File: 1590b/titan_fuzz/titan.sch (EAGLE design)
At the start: 60 parts, among them J1 DC_MONO, Q1 2N5088, Q2 2N5088, Q3 2N5088, Q4 2N5088

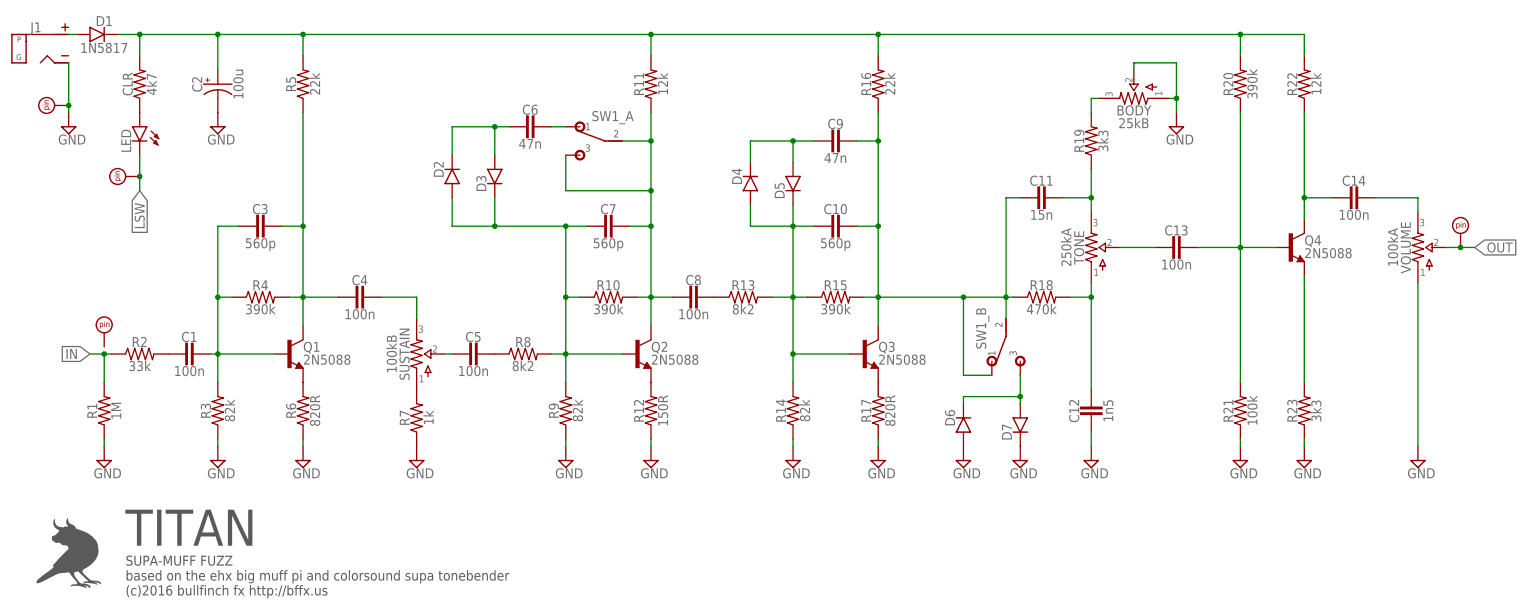
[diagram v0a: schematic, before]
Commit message: updated library + logos
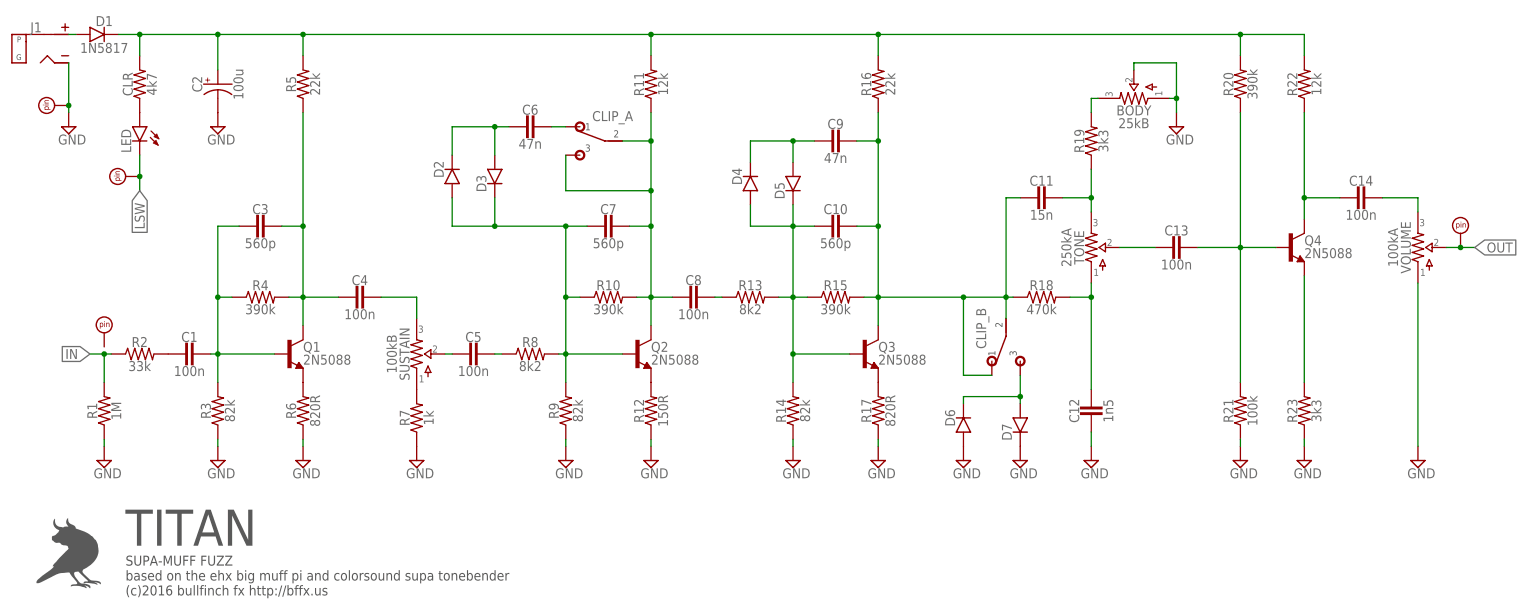
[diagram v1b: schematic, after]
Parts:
- renumbered SW1 to CLIP
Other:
- moved on the sheet: C14, R13, R8
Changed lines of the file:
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@@
 <setting verticaltext="up"/>
 </settings>
-<grid distance="0.05" unitdist="inch" unit="inch" style="lines" multiple="2" display="no" altdistance="0.01" altunitdist="inch" altunit="inch"/>
+<grid distance="0.1" unitdist="inch" unit="inch" style="lines" multiple="1" display="no" altdistance="0.01" altunitdist="inch" altunit="inch"/>
 <layers>
 <layer number="1" name="Top" color="4" fill="1" visible="no" active="no"/>
@@
 <part name="GND11" library="supply pins" deviceset="GND" device=""/>
 <part name="GND12" library="supply pins" deviceset="GND" device=""/>
-<part name="SW1" library="switches" deviceset="DPDT" device="PADS"/>
+<part name="CLIP" library="switches" deviceset="DPDT" device="PADS"/>
 <part name="BF1" library="logos" deviceset="BULLFINCH" device=""/>
 <part name="IN" library="supply pins" deviceset="PAD" device="SQR"/>
@@
 <instance part="R7" gate="G$1" x="77.47" y="34.29" rot="R90"/>
 <instance part="C5" gate="G$1" x="87.63" y="45.72"/>
-<instance part="R8" gate="G$1" x="96.52" y="45.72"/>
+<instance part="R8" gate="G$1" x="97.79" y="45.72"/>
 <instance part="R9" gate="G$1" x="104.14" y="35.56" rot="R90"/>
 <instance part="Q2" gate="G$1" x="116.84" y="45.72"/>
@@
 <instance part="R10" gate="G$1" x="111.76" y="55.88"/>
 <instance part="C8" gate="G$1" x="127" y="55.88"/>
-<instance part="R13" gate="G$1" x="135.89" y="55.88"/>
+<instance part="R13" gate="G$1" x="137.16" y="55.88"/>
 <instance part="C7" gate="G$1" x="111.76" y="68.58"/>
 <instance part="C6" gate="G$1" x="97.79" y="86.36"/>
@@
 <instance part="R22" gate="G$1" x="236.22" y="93.98" rot="R90"/>
 <instance part="R23" gate="G$1" x="236.22" y="35.56" rot="R90"/>
-<instance part="C14" gate="G$1" x="245.11" y="73.66"/>
+<instance part="C14" gate="G$1" x="246.38" y="73.66"/>
 <instance part="VOLUME" gate="G$1" x="256.54" y="64.77"/>
 <instance part="J1" gate="DC" x="10.16" y="100.33"/>
@@
 <instance part="GND11" gate="GND" x="175.26" y="26.67"/>
 <instance part="GND12" gate="GND" x="185.42" y="26.67"/>
-<instance part="SW1" gate="_A" x="109.22" y="83.82" rot="MR270"/>
-<instance part="SW1" gate="_B" x="182.88" y="46.99" rot="MR180"/>
+<instance part="CLIP" gate="_A" x="109.22" y="83.82" rot="MR270"/>
+<instance part="CLIP" gate="_B" x="182.88" y="46.99" rot="MR180"/>
 <instance part="BF1" gate="G$1" x="15.24" y="10.16"/>
 <instance part="IN" gate="G$1" x="21.59" y="46.99"/>
@@
 <pinref part="C8" gate="G$1" pin="1"/>
 <pinref part="R13" gate="G$1" pin="1"/>
+<wire x1="132.08" y1="55.88" x2="130.81" y2="55.88" width="0.1524" layer="91"/>
 </segment>
 </net>
@@
 <pinref part="C5" gate="G$1" pin="1"/>
 <pinref part="R8" gate="G$1" pin="1"/>
+<wire x1="92.71" y1="45.72" x2="91.44" y2="45.72" width="0.1524" layer="91"/>
 </segment>
 </net>
@@
 <junction x="119.38" y="55.88"/>
 <wire x1="119.38" y1="55.88" x2="123.19" y2="55.88" width="0.1524" layer="91"/>
-<pinref part="SW1" gate="_A" pin="2"/>
+<pinref part="CLIP" gate="_A" pin="2"/>
 <wire x1="114.3" y1="83.82" x2="119.38" y2="83.82" width="0.1524" layer="91"/>
 <junction x="119.38" y="83.82"/>
-<pinref part="SW1" gate="_A" pin="3"/>
+<pinref part="CLIP" gate="_A" pin="3"/>
 <wire x1="104.14" y1="81.28" x2="104.14" y2="74.93" width="0.1524" layer="91"/>
 <wire x1="104.14" y1="74.93" x2="119.38" y2="74.93" width="0.1524" layer="91"/>
@@
 <pinref part="R8" gate="G$1" pin="2"/>
 <pinref part="Q2" gate="G$1" pin="B"/>
-<wire x1="101.6" y1="45.72" x2="104.14" y2="45.72" width="0.1524" layer="91"/>
+<wire x1="102.87" y1="45.72" x2="104.14" y2="45.72" width="0.1524" layer="91"/>
 <wire x1="104.14" y1="45.72" x2="114.3" y2="45.72" width="0.1524" layer="91"/>
 <wire x1="104.14" y1="68.58" x2="104.14" y2="55.88" width="0.1524" layer="91"/>
@@
 <wire x1="182.88" y1="73.66" x2="185.42" y2="73.66" width="0.1524" layer="91"/>
 <junction x="182.88" y="55.88"/>
-<pinref part="SW1" gate="_B" pin="2"/>
+<pinref part="CLIP" gate="_B" pin="2"/>
 <wire x1="175.26" y1="55.88" x2="182.88" y2="55.88" width="0.1524" layer="91"/>
 <wire x1="182.88" y1="55.88" x2="182.88" y2="52.07" width="0.1524" layer="91"/>
-<pinref part="SW1" gate="_B" pin="1"/>
+<pinref part="CLIP" gate="_B" pin="1"/>
 <wire x1="180.34" y1="41.91" x2="175.26" y2="41.91" width="0.1524" layer="91"/>
 <wire x1="175.26" y1="41.91" x2="175.26" y2="55.88" width="0.1524" layer="91"/>
@@
 <junction x="144.78" y="55.88"/>
 <pinref part="R13" gate="G$1" pin="2"/>
-<wire x1="144.78" y1="55.88" x2="140.97" y2="55.88" width="0.1524" layer="91"/>
+<wire x1="144.78" y1="55.88" x2="142.24" y2="55.88" width="0.1524" layer="91"/>
 </segment>
 </net>
@@
 <pinref part="C14" gate="G$1" pin="2"/>
 <wire x1="236.22" y1="73.66" x2="236.22" y2="69.85" width="0.1524" layer="91"/>
-<wire x1="241.3" y1="73.66" x2="236.22" y2="73.66" width="0.1524" layer="91"/>
+<wire x1="242.57" y1="73.66" x2="236.22" y2="73.66" width="0.1524" layer="91"/>
 <junction x="236.22" y="73.66"/>
 </segment>
@@
 <pinref part="C14" gate="G$1" pin="1"/>
 <pinref part="VOLUME" gate="G$1" pin="3"/>
-<wire x1="248.92" y1="73.66" x2="256.54" y2="73.66" width="0.1524" layer="91"/>
+<wire x1="250.19" y1="73.66" x2="256.54" y2="73.66" width="0.1524" layer="91"/>
 <wire x1="256.54" y1="73.66" x2="256.54" y2="71.12" width="0.1524" layer="91"/>
 </segment>
@@
 <net name="N$24" class="0">
 <segment>
-<pinref part="SW1" gate="_B" pin="3"/>
+<pinref part="CLIP" gate="_B" pin="3"/>
 <pinref part="D7" gate="G$1" pin="A"/>
 <wire x1="185.42" y1="41.91" x2="185.42" y2="38.1" width="0.1524" layer="91"/>
@@
 <segment>
 <pinref part="C6" gate="G$1" pin="1"/>
-<pinref part="SW1" gate="_A" pin="1"/>
+<pinref part="CLIP" gate="_A" pin="1"/>
 <wire x1="101.6" y1="86.36" x2="104.14" y2="86.36" width="0.1524" layer="91"/>
 </segment>
